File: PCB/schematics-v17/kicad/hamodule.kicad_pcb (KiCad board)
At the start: 2 copper layers, 76.7 x 84.3 mm, 85 parts, among them J1 2604-1104, J10 EspSense, J11 Conn_01x02_Male, J12 DoNotConnect->, J2 2604-1102, J3 USB_C_Receptacle, J4 ESP Relays, J5 Current Jumper, J6 GND 3.3V, J7 Conn_01x02, J8 Current Jumper, J9 2604-1104, K1 PCN-105D, K2 PCN-105D, K3 PCN-105D, K4 PCN-105D, Q1 SS8050-SMD, Q2 SS8050, SW1 EN, SW2 IO0, U1 ULN2003A, U2 ESP32-WROOM-32E, U4 LD1117AV33_TO220, U5 MCP9700T-ETT, U6 LDA210-PDIP, U7 LDA210-PDIP, U8 CP2102N-A01-GQFN28

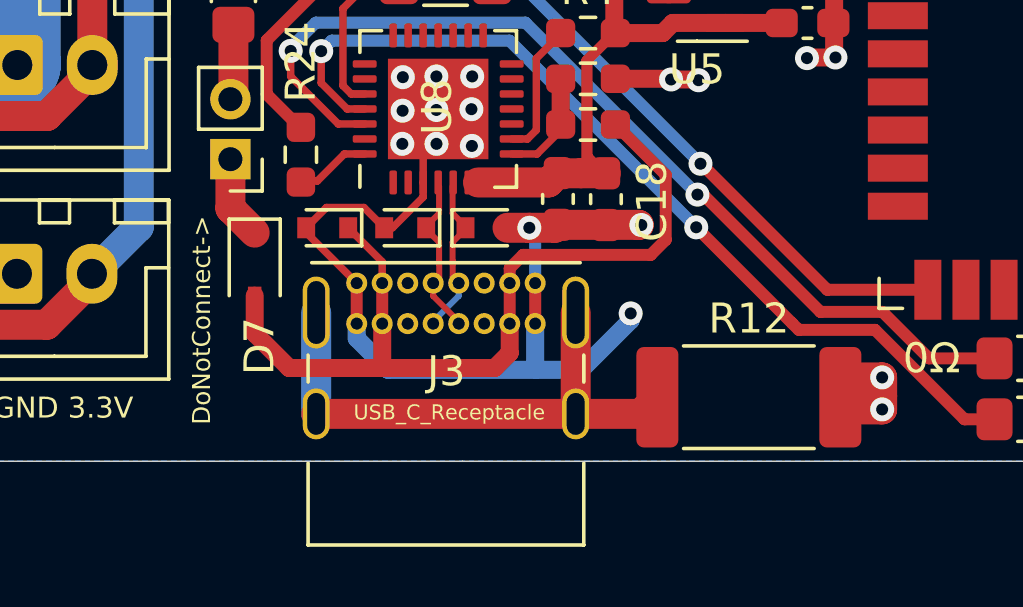
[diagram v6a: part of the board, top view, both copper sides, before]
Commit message: adding missing resistors to the USB port
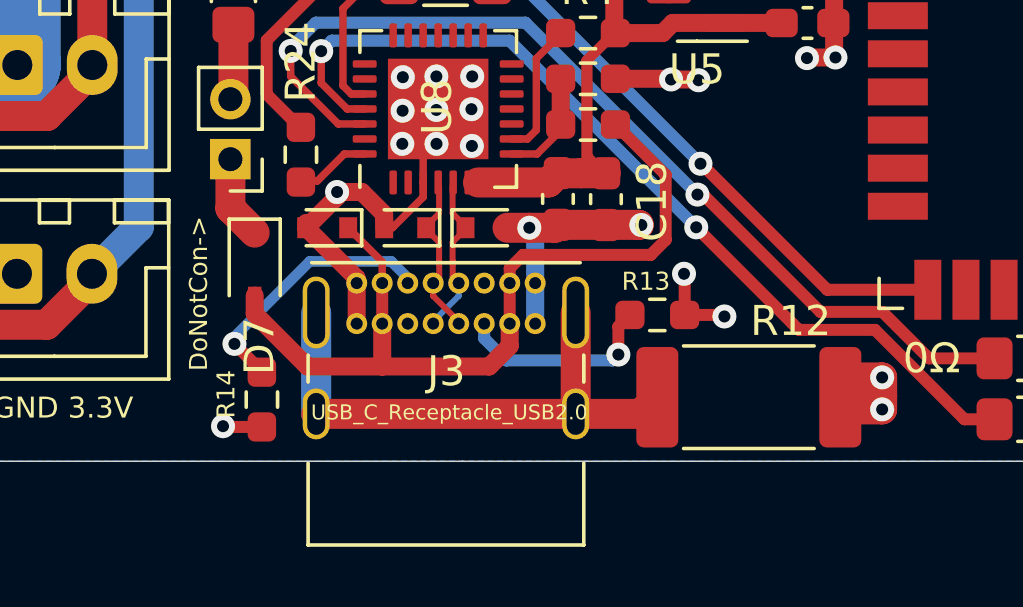
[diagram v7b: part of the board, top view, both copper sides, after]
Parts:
- added R13: 5.11kΩ, Resistor_SMD:R_0603_1608Metric_Pad0.98x0.95mm_HandSolder, F.Cu at (168.3, 146.8)
- added R14: 5.11kΩ, Resistor_SMD:R_0603_1608Metric_Pad0.98x0.95mm_HandSolder, F.Cu at (155.2, 149.6)
- J12: value DoNotConnect-> -> DoNotCon->
- J3: value USB_C_Receptacle -> USB_C_Receptacle_USB2.0
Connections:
- J3 pad A5: unconnected-(J3-PadA5) -> Net-(J3-PadA5)
- J3 pad B5: unconnected-(J3-PadB5) -> Net-(J3-PadB5)
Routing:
- net Net-(J3-PadA5): track 0.00 -> 8.78 mm, vias 0 -> 1
- net GND: track 221.5 -> 214.0 mm, vias 57 -> 60
- net Net-(J3-PadB5): track 0.00 -> 6.83 mm, vias 0 -> 1
- net VBUS: track 28.5 -> 27.9 mm

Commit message: fixing EspRel wrong naming
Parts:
- R13, R14: value 5.11kΩ -> 5.1kΩ
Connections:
- J4 pad 1: EspRel4 -> EspRel1
- J4 pad 2: EspRel3 -> EspRel2
- J4 pad 3: EspRel2 -> EspRel3
- J4 pad 4: EspRel1 -> EspRel4
- U1 pad 4: EspRel4 -> EspRel1
- U1 pad 5: EspRel3 -> EspRel2
- U1 pad 6: EspRel2 -> EspRel3
- U1 pad 7: EspRel1 -> EspRel4
- U2 pad 10: EspRel1 -> EspRel4
- U2 pad 11: EspRel2 -> EspRel3
- U2 pad 12: EspRel3 -> EspRel2
- U2 pad 14: EspRel4 -> EspRel1
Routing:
- net EspRel4: track 33.3 -> 24.4 mm
- net EspRel1: track 24.4 -> 33.3 mm
- net EspRel3: track 28.5 -> 25.5 mm
- net EspRel2: track 25.5 -> 28.5 mm
